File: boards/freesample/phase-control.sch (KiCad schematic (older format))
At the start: 0 parts

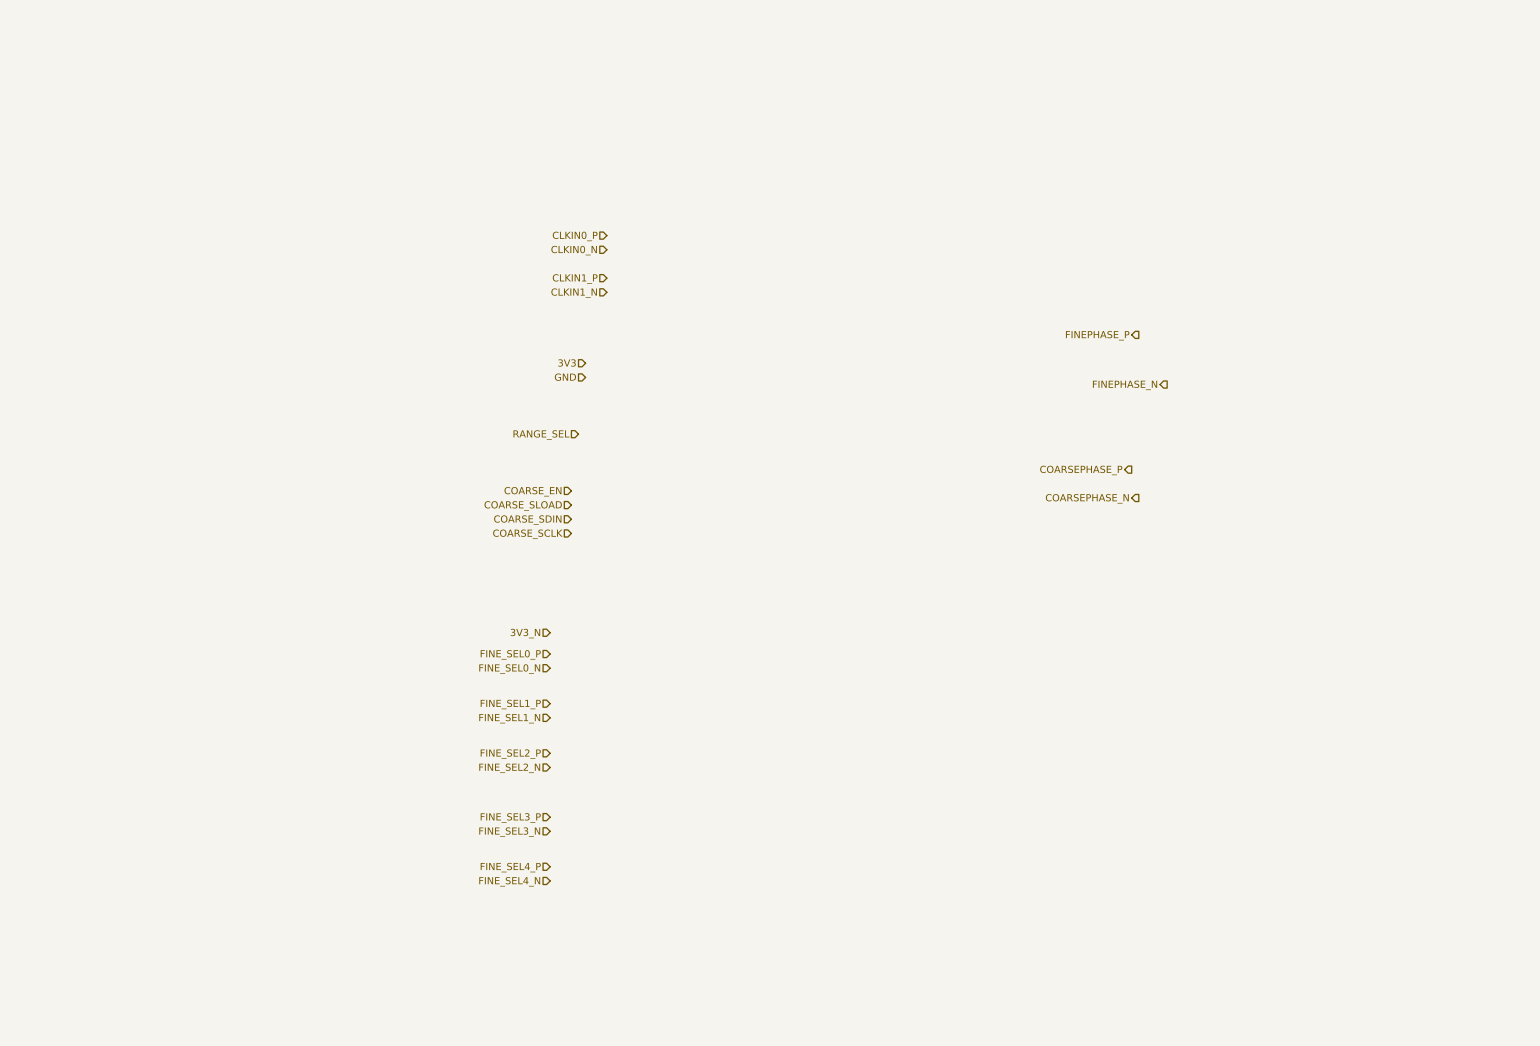
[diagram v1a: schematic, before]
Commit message: Continued work on FREESAMPLE schematic including PSU.
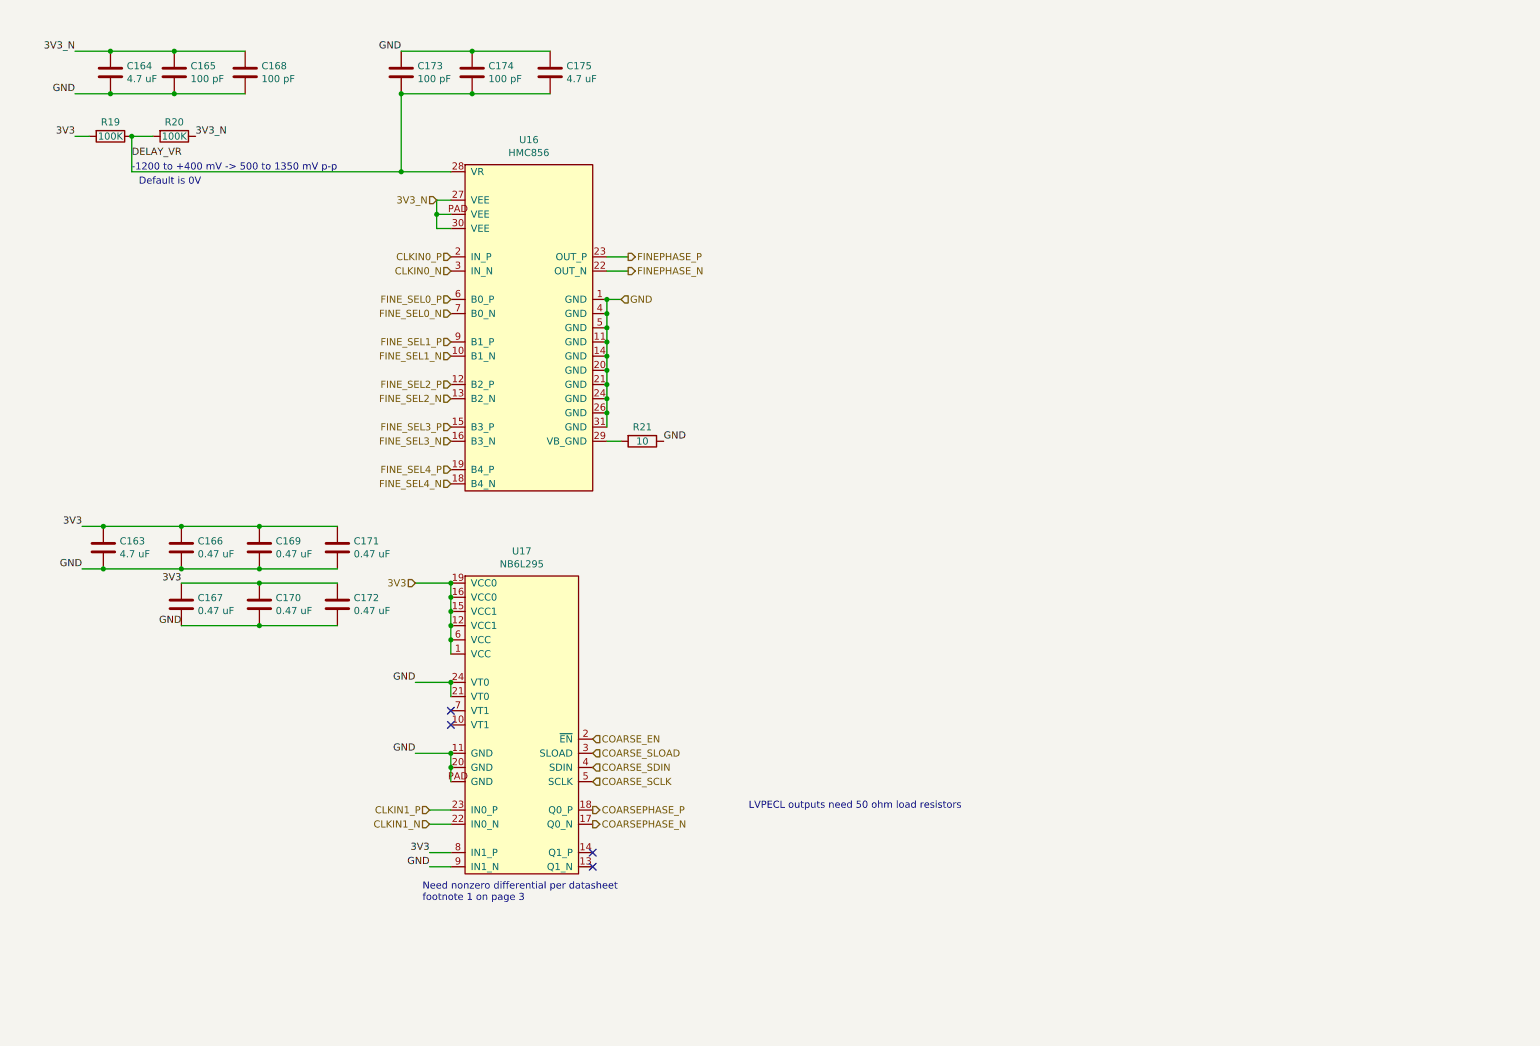
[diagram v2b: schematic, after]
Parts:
- added C163, C164, C175: 4.7 uF, symbol device:C
- added C165, C168, C173, C174: 100 pF, symbol device:C
- added C166, C167, C169, C170, C171, C172: 0.47 uF, symbol device:C
- added R19, R20: 100K, symbol device:R
- added R21: 10, symbol device:R
- added U16: HMC856, symbol special-azonenberg:HMC856
- added U17: NB6L295, symbol special-azonenberg:NB6L295
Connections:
- net 3V3: now also C163.1, C166.1, C167.1, C169.1, C170.1, C171.1, C172.1, R19.2, U17.1 (VCC), U17.12 (VCC1), U17.15 (VCC1), U17.16 (VCC0), U17.19 (VCC0), U17.6 (VCC), U17.8 (IN1_P)
- net 3V3_N: now also C164.1, C165.1, C168.1, R20.1, U16.27 (VEE), U16.30 (VEE), U16.PAD (VEE)
- net CLKIN0_N: now also U16.3 (IN_N)
- net CLKIN0_P: now also U16.2 (IN_P)
- net CLKIN1_N: now also U17.22 (IN0_N)
- net CLKIN1_P: now also U17.23 (IN0_P)
- net COARSEPHASE_N: now also U17.17 (Q0_N)
- net COARSEPHASE_P: now also U17.18 (Q0_P)
- net COARSE_EN: now also U17.2 (~EN)
- net COARSE_SCLK: now also U17.5 (SCLK)
- net COARSE_SDIN: now also U17.4 (SDIN)
- net COARSE_SLOAD: now also U17.3 (SLOAD)
- net FINEPHASE_N: now also U16.22 (OUT_N)
- net FINEPHASE_P: now also U16.23 (OUT_P)
- net FINE_SEL0_N: now also U16.7 (B0_N)
- net FINE_SEL0_P: now also U16.6 (B0_P)
- net FINE_SEL1_N: now also U16.10 (B1_N)
- net FINE_SEL1_P: now also U16.9 (B1_P)
- net FINE_SEL2_N: now also U16.13 (B2_N)
- net FINE_SEL2_P: now also U16.12 (B2_P)
- net FINE_SEL3_N: now also U16.16 (B3_N)
- net FINE_SEL3_P: now also U16.15 (B3_P)
- net FINE_SEL4_N: now also U16.18 (B4_N)
- net FINE_SEL4_P: now also U16.19 (B4_P)
- net GND: now also C163.2, C164.2, C165.2, C166.2, C167.2, C168.2, C169.2, C170.2, C171.2, C172.2, C173.1, C174.1, C175.1, R21.1, U16.1 (GND), U16.11 (GND), U16.14 (GND), U16.20 (GND), U16.21 (GND), U16.24 (GND), U16.26 (GND), U16.31 (GND), U16.4 (GND), U16.5 (GND), U17.11 (GND), U17.20 (GND), U17.21 (VT0), U17.24 (VT0), U17.9 (IN1_N), U17.PAD (GND)
- new net: R21.2, U16.29 (VB_GND)
- new net DELAY_VR: C173.2, C174.2, C175.2, R19.1, R20.2, U16.28 (VR)
- no-connect marks 0 -> 4
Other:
- note added: "-1200 to +400 mV -> 500 to 1350 mV p-p"
- note added: "Default is 0V"
- note added: "LVPECL outputs need 50 ohm load resistors"
- note added: "Need nonzero differential per datasheet\nfootnote 1 on page 3"

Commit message: Lots more work on PSU and sch readability improvements
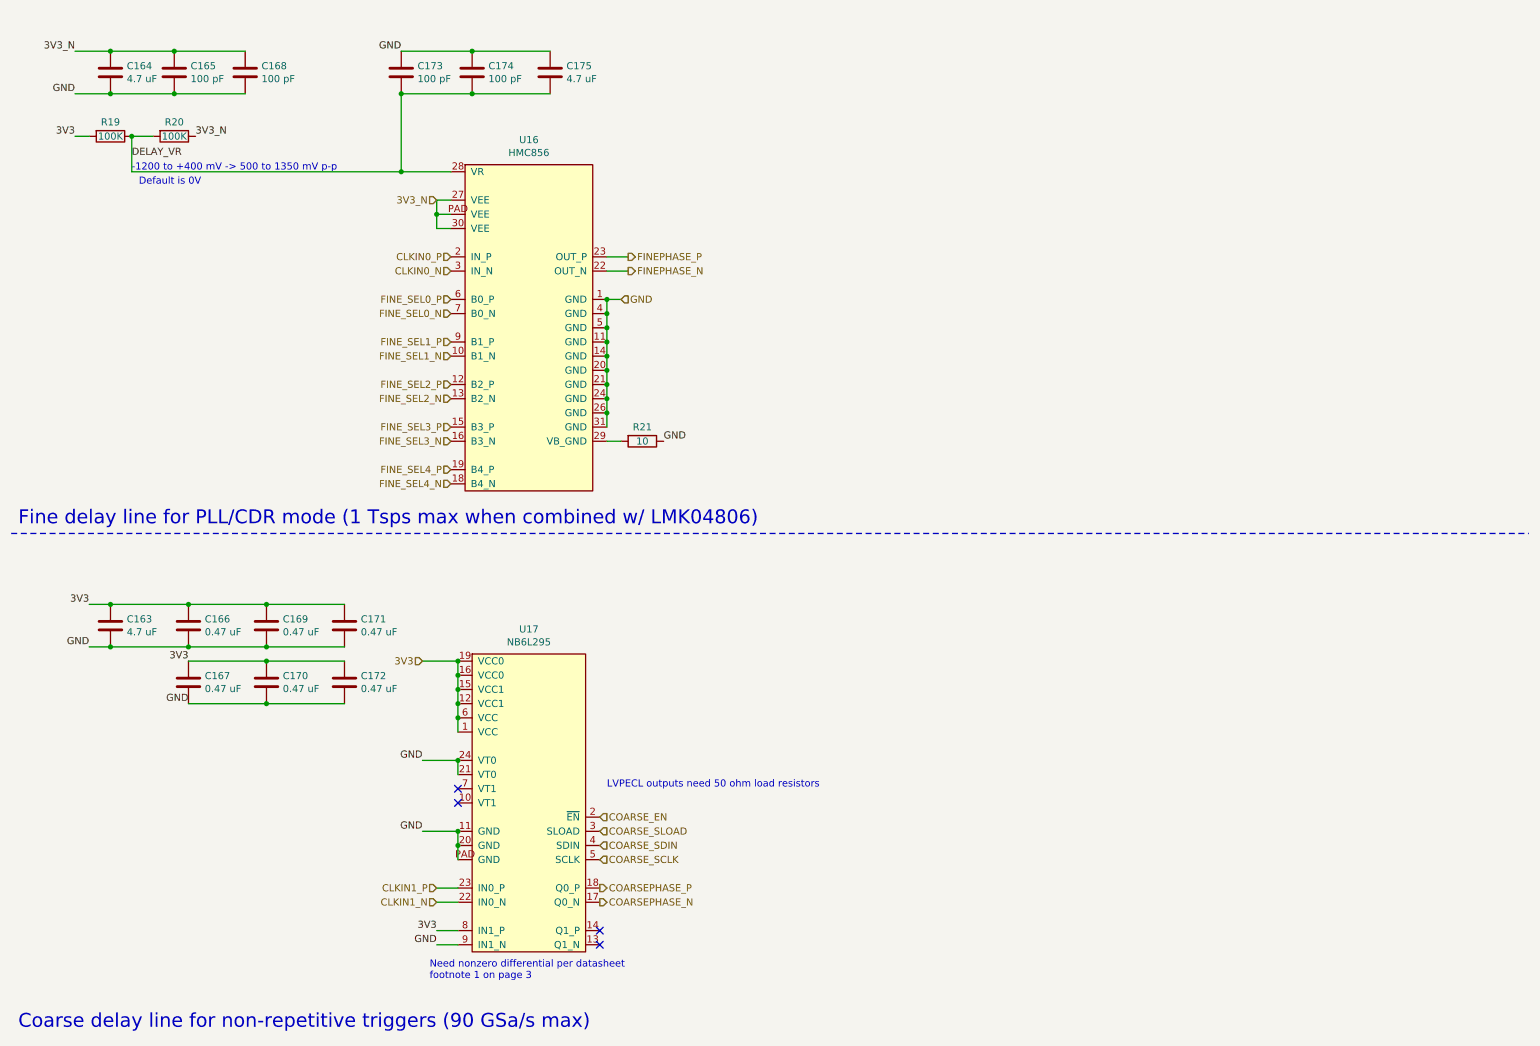
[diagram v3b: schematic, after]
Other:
- note added: "Coarse delay line for non-repetitive triggers (90 GSa/s max)"
- note added: "Fine delay line for PLL/CDR mode (1 Tsps max when combined w/ LMK04806)"
- moved on the sheet: C163, C166, C167, C169, C170, C171, C172, U17
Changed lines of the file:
@@
 Text HLabel 4850 2350 2    50   Output ~ 0
 FINEPHASE_N
-Text HLabel 4600 6150 2    50   Output ~ 0
+Text HLabel 4650 6700 2    50   Output ~ 0
 COARSEPHASE_P
-Text HLabel 4600 6250 2    50   Output ~ 0
+Text HLabel 4650 6800 2    50   Output ~ 0
 COARSEPHASE_N
 Text HLabel 3600 2250 0    50   Input ~ 0
@@
 Text HLabel 3600 2350 0    50   Input ~ 0
 CLKIN0_N
-Text HLabel 3350 4550 0    50   Input ~ 0
+Text HLabel 3400 5100 0    50   Input ~ 0
 3V3
 Text HLabel 4800 2550 2    50   Input ~ 0
 GND
-Text HLabel 4600 5650 2    50   Input ~ 0
+Text HLabel 4650 6200 2    50   Input ~ 0
 COARSE_EN
-Text HLabel 4600 5750 2    50   Input ~ 0
+Text HLabel 4650 6300 2    50   Input ~ 0
 COARSE_SLOAD
-Text HLabel 4600 5850 2    50   Input ~ 0
+Text HLabel 4650 6400 2    50   Input ~ 0
 COARSE_SDIN
-Text HLabel 4600 5950 2    50   Input ~ 0
+Text HLabel 4650 6500 2    50   Input ~ 0
 COARSE_SCLK
 Text HLabel 3500 1850 0    50   Input ~ 0
@@
 L special-azonenberg:NB6L295 U17
 U 1 1 5CA9AC29
-P 3700 6600
-F 0 "U17" H 4100 8875 50  0000 C CNN
-F 1 "NB6L295" H 4100 8784 50  0000 C CNN
-F 2 "" H 3700 6600 50  0001 C CNN
-F 3 "" H 3700 6600 50  0001 C CNN
-	1    3700 6600
-	1    0    0    -1
-$EndComp
-Wire Wire Line
-	3350 4550 3600 4550
-Wire Wire Line
-	3600 4550 3600 4650
-Connection ~ 3600 4550
-Connection ~ 3600 4650
-Wire Wire Line
-	3600 4650 3600 4750
-Connection ~ 3600 4750
-Wire Wire Line
-	3600 4750 3600 4850
-Connection ~ 3600 4850
-Wire Wire Line
-	3600 4850 3600 4950
-Connection ~ 3600 4950
-Wire Wire Line
-	3600 4950 3600 5050
-Text Label 3350 5250 2    50   ~ 0
-GND
-Wire Wire Line
-	3350 5250 3600 5250
-Wire Wire Line
-	3600 5250 3600 5350
-Connection ~ 3600 5250
-Wire Wire Line
-	3600 5750 3600 5850
-Connection ~ 3600 5850
-Wire Wire Line
-	3600 5850 3600 5950
-NoConn ~ 4600 6450
-NoConn ~ 4600 6550
-Text Notes 5700 6150 0    50   ~ 0
+P 3750 7150
+F 0 "U17" H 4150 9425 50  0000 C CNN
+F 1 "NB6L295" H 4150 9334 50  0000 C CNN
+F 2 "" H 3750 7150 50  0001 C CNN
+F 3 "" H 3750 7150 50  0001 C CNN
+	1    3750 7150
+	1    0    0    -1
+$EndComp
+Wire Wire Line
+	3400 5100 3650 5100
+Wire Wire Line
+	3650 5100 3650 5200
+Connection ~ 3650 5100
+Connection ~ 3650 5200
+Wire Wire Line
+	3650 5200 3650 5300
+Connection ~ 3650 5300
+Wire Wire Line
+	3650 5300 3650 5400
+Connection ~ 3650 5400
+Wire Wire Line
+	3650 5400 3650 5500
+Connection ~ 3650 5500
+Wire Wire Line
+	3650 5500 3650 5600
+Text Label 3400 5800 2    50   ~ 0
+GND
+Wire Wire Line
+	3400 5800 3650 5800
+Wire Wire Line
+	3650 5800 3650 5900
+Connection ~ 3650 5800
+Wire Wire Line
+	3650 6300 3650 6400
+Connection ~ 3650 6400
+Wire Wire Line
+	3650 6400 3650 6500
+NoConn ~ 4650 7000
+NoConn ~ 4650 7100
+Text Notes 4700 6000 0    50   ~ 0
 LVPECL outputs need 50 ohm load resistors
 Wire Wire Line
-	3600 6250 3450 6250
-Wire Wire Line
-	3450 6150 3600 6150
-Text HLabel 3450 6250 0    50   Input ~ 0
+	3650 6800 3500 6800
+Wire Wire Line
+	3500 6700 3650 6700
+Text HLabel 3500 6800 0    50   Input ~ 0
 CLKIN1_N
-Text HLabel 3450 6150 0    50   Input ~ 0
+Text HLabel 3500 6700 0    50   Input ~ 0
 CLKIN1_P
 $Comp
 L device:C C163
 U 1 1 5CAAE7E5
-P 1150 4300
-F 0 "C163" H 1265 4346 50  0000 L CNN
-F 1 "4.7 uF" H 1265 4255 50  0000 L CNN
-F 2 "" H 1188 4150 50  0001 C CNN
-F 3 "" H 1150 4300 50  0001 C CNN
-	1    1150 4300
-	1    0    0    -1
-$EndComp
-Text Label 1000 4150 2    50   ~ 0
+P 1200 4850
+F 0 "C163" H 1315 4896 50  0000 L CNN
+F 1 "4.7 uF" H 1315 4805 50  0000 L CNN
+F 2 "" H 1238 4700 50  0001 C CNN
+F 3 "" H 1200 4850 50  0001 C CNN
+	1    1200 4850
+	1    0    0    -1
+$EndComp
+Text Label 1050 4700 2    50   ~ 0
 3V3
-Text Label 1000 4450 2    50   ~ 0
+Text Label 1050 5000 2    50   ~ 0
 GND
 $Comp
 L device:C C166
 U 1 1 5CAAFCC4
-P 1700 4300
-F 0 "C166" H 1815 4346 50  0000 L CNN
-F 1 "0.47 uF" H 1815 4255 50  0000 L CNN
-F 2 "" H 1738 4150 50  0001 C CNN
-F 3 "" H 1700 4300 50  0001 C CNN
-	1    1700 4300
+P 1750 4850
+F 0 "C166" H 1865 4896 50  0000 L CNN
+F 1 "0.47 uF" H 1865 4805 50  0000 L CNN
+F 2 "" H 1788 4700 50  0001 C CNN
+F 3 "" H 1750 4850 50  0001 C CNN
+	1    1750 4850
 	1    0    0    -1
 $EndComp
@@
 L device:C C169
 U 1 1 5CAB0185
-P 2250 4300
-F 0 "C169" H 2365 4346 50  0000 L CNN
-F 1 "0.47 uF" H 2365 4255 50  0000 L CNN
-F 2 "" H 2288 4150 50  0001 C CNN
-F 3 "" H 2250 4300 50  0001 C CNN
-	1    2250 4300
+P 2300 4850
+F 0 "C169" H 2415 4896 50  0000 L CNN
+F 1 "0.47 uF" H 2415 4805 50  0000 L CNN
+F 2 "" H 2338 4700 50  0001 C CNN
+F 3 "" H 2300 4850 50  0001 C CNN
+	1    2300 4850
 	1    0    0    -1
 $EndComp
@@
 L device:C C171
 U 1 1 5CAB03B7
-P 2800 4300
-F 0 "C171" H 2915 4346 50  0000 L CNN
-F 1 "0.47 uF" H 2915 4255 50  0000 L CNN
-F 2 "" H 2838 4150 50  0001 C CNN
-F 3 "" H 2800 4300 50  0001 C CNN
-	1    2800 4300
-	1    0    0    -1
-$EndComp
-Wire Wire Line
-	2800 4150 2250 4150
-Connection ~ 1150 4150
-Wire Wire Line
-	1150 4150 1000 4150
-Connection ~ 1700 4150
-Wire Wire Line
-	1700 4150 1150 4150
-Connection ~ 2250 4150
-Wire Wire Line
-	2250 4150 1700 4150
-Wire Wire Line
-	1000 4450 1150 4450
-Connection ~ 1150 4450
-Wire Wire Line
-	1150 4450 1700 4450
-Connection ~ 1700 4450
-Wire Wire Line
-	1700 4450 2250 4450
-Connection ~ 2250 4450
-Wire Wire Line
-	2250 4450 2800 4450
+P 2850 4850
+F 0 "C171" H 2965 4896 50  0000 L CNN
+F 1 "0.47 uF" H 2965 4805 50  0000 L CNN
+F 2 "" H 2888 4700 50  0001 C CNN
+F 3 "" H 2850 4850 50  0001 C CNN
+	1    2850 4850
+	1    0    0    -1
+$EndComp
+Wire Wire Line
+	2850 4700 2300 4700
+Connection ~ 1200 4700
+Wire Wire Line
+	1200 4700 1050 4700
+Connection ~ 1750 4700
+Wire Wire Line
+	1750 4700 1200 4700
+Connection ~ 2300 4700
+Wire Wire Line
+	2300 4700 1750 4700
+Wire Wire Line
+	1050 5000 1200 5000
+Connection ~ 1200 5000
+Wire Wire Line
+	1200 5000 1750 5000
+Connection ~ 1750 5000
+Wire Wire Line
+	1750 5000 2300 5000
+Connection ~ 2300 5000
+Wire Wire Line
+	2300 5000 2850 5000
 $Comp
 L device:C C172
 U 1 1 5CAB20BA
-P 2800 4700
-F 0 "C172" H 2915 4746 50  0000 L CNN
-F 1 "0.47 uF" H 2915 4655 50  0000 L CNN
-F 2 "" H 2838 4550 50  0001 C CNN
-F 3 "" H 2800 4700 50  0001 C CNN
-	1    2800 4700
+P 2850 5250
+F 0 "C172" H 2965 5296 50  0000 L CNN
+F 1 "0.47 uF" H 2965 5205 50  0000 L CNN
+F 2 "" H 2888 5100 50  0001 C CNN
+F 3 "" H 2850 5250 50  0001 C CNN
+	1    2850 5250
 	1    0    0    -1
 $EndComp
@@
 L device:C C170
 U 1 1 5CAB26E8
-P 2250 4700
-F 0 "C170" H 2365 4746 50  0000 L CNN
-F 1 "0.47 uF" H 2365 4655 50  0000 L CNN
-F 2 "" H 2288 4550 50  0001 C CNN
-F 3 "" H 2250 4700 50  0001 C CNN
-	1    2250 4700
+P 2300 5250
+F 0 "C170" H 2415 5296 50  0000 L CNN
+F 1 "0.47 uF" H 2415 5205 50  0000 L CNN
+F 2 "" H 2338 5100 50  0001 C CNN
+F 3 "" H 2300 5250 50  0001 C CNN
+	1    2300 5250
 	1    0    0    -1
 $EndComp
@@
 L device:C C167
 U 1 1 5CAB2BEF
-P 1700 4700
-F 0 "C167" H 1815 4746 50  0000 L CNN
-F 1 "0.47 uF" H 1815 4655 50  0000 L CNN
-F 2 "" H 1738 4550 50  0001 C CNN
-F 3 "" H 1700 4700 50  0001 C CNN
-	1    1700 4700
-	1    0    0    -1
-$EndComp
-Wire Wire Line
-	1700 4550 2250 4550
-Connection ~ 2250 4550
-Wire Wire Line
-	2250 4550 2800 4550
-Wire Wire Line
-	2800 4850 2250 4850
-Connection ~ 2250 4850
-Wire Wire Line
-	2250 4850 1700 4850
-Text Label 1700 4550 2    50   ~ 0
+P 1750 5250
+F 0 "C167" H 1865 5296 50  0000 L CNN
+F 1 "0.47 uF" H 1865 5205 50  0000 L CNN
+F 2 "" H 1788 5100 50  0001 C CNN
+F 3 "" H 1750 5250 50  0001 C CNN
+	1    1750 5250
+	1    0    0    -1
+$EndComp
+Wire Wire Line
+	1750 5100 2300 5100
+Connection ~ 2300 5100
+Wire Wire Line
+	2300 5100 2850 5100
+Wire Wire Line
+	2850 5400 2300 5400
+Connection ~ 2300 5400
+Wire Wire Line
+	2300 5400 1750 5400
+Text Label 1750 5100 2    50   ~ 0
 3V3
-Text Label 1700 4850 2    50   ~ 0
-GND
-Text Label 3450 6450 2    50   ~ 0
+Text Label 1750 5400 2    50   ~ 0
+GND
+Text Label 3500 7000 2    50   ~ 0
 3V3
 Wire Wire Line
-	3450 6450 3600 6450
-NoConn ~ 3600 5450
-NoConn ~ 3600 5550
-Text Label 3350 5750 2    50   ~ 0
-GND
-Wire Wire Line
-	3350 5750 3600 5750
-Connection ~ 3600 5750
-Text Label 3450 6550 2    50   ~ 0
-GND
-Wire Wire Line
-	3450 6550 3600 6550
-Text Notes 3400 6800 0    50   ~ 0
+	3500 7000 3650 7000
+NoConn ~ 3650 6000
+NoConn ~ 3650 6100
+Text Label 3400 6300 2    50   ~ 0
+GND
+Wire Wire Line
+	3400 6300 3650 6300
+Connection ~ 3650 6300
+Text Label 3500 7100 2    50   ~ 0
+GND
+Wire Wire Line
+	3500 7100 3650 7100
+Text Notes 3450 7350 0    50   ~ 0
 Need nonzero differential per datasheet\nfootnote 1 on page 3
+Wire Notes Line width 20 style solid
+	500  4200 11200 4200
+Text Notes 550  4150 0    98   ~ 0
+Fine delay line for PLL/CDR mode (1 Tsps max when combined w/ LMK04806)
+Text Notes 550  7700 0    98   ~ 0
+Coarse delay line for non-repetitive triggers (90 GSa/s max)
 $EndSCHEMATC
